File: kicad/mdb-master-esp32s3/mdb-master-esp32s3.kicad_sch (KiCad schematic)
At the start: 32 parts, among them J1 MDB_Connector, J2 Barrel_Jack, J3 USB_C_Receptacle_USB2.0_16P, J4 Conn_02x11_Odd_Even, Q1 BC807, SW1 SW_Push, U1 ESP32-S3R8, U2 AMS1117-3.3, Y1 40000hz

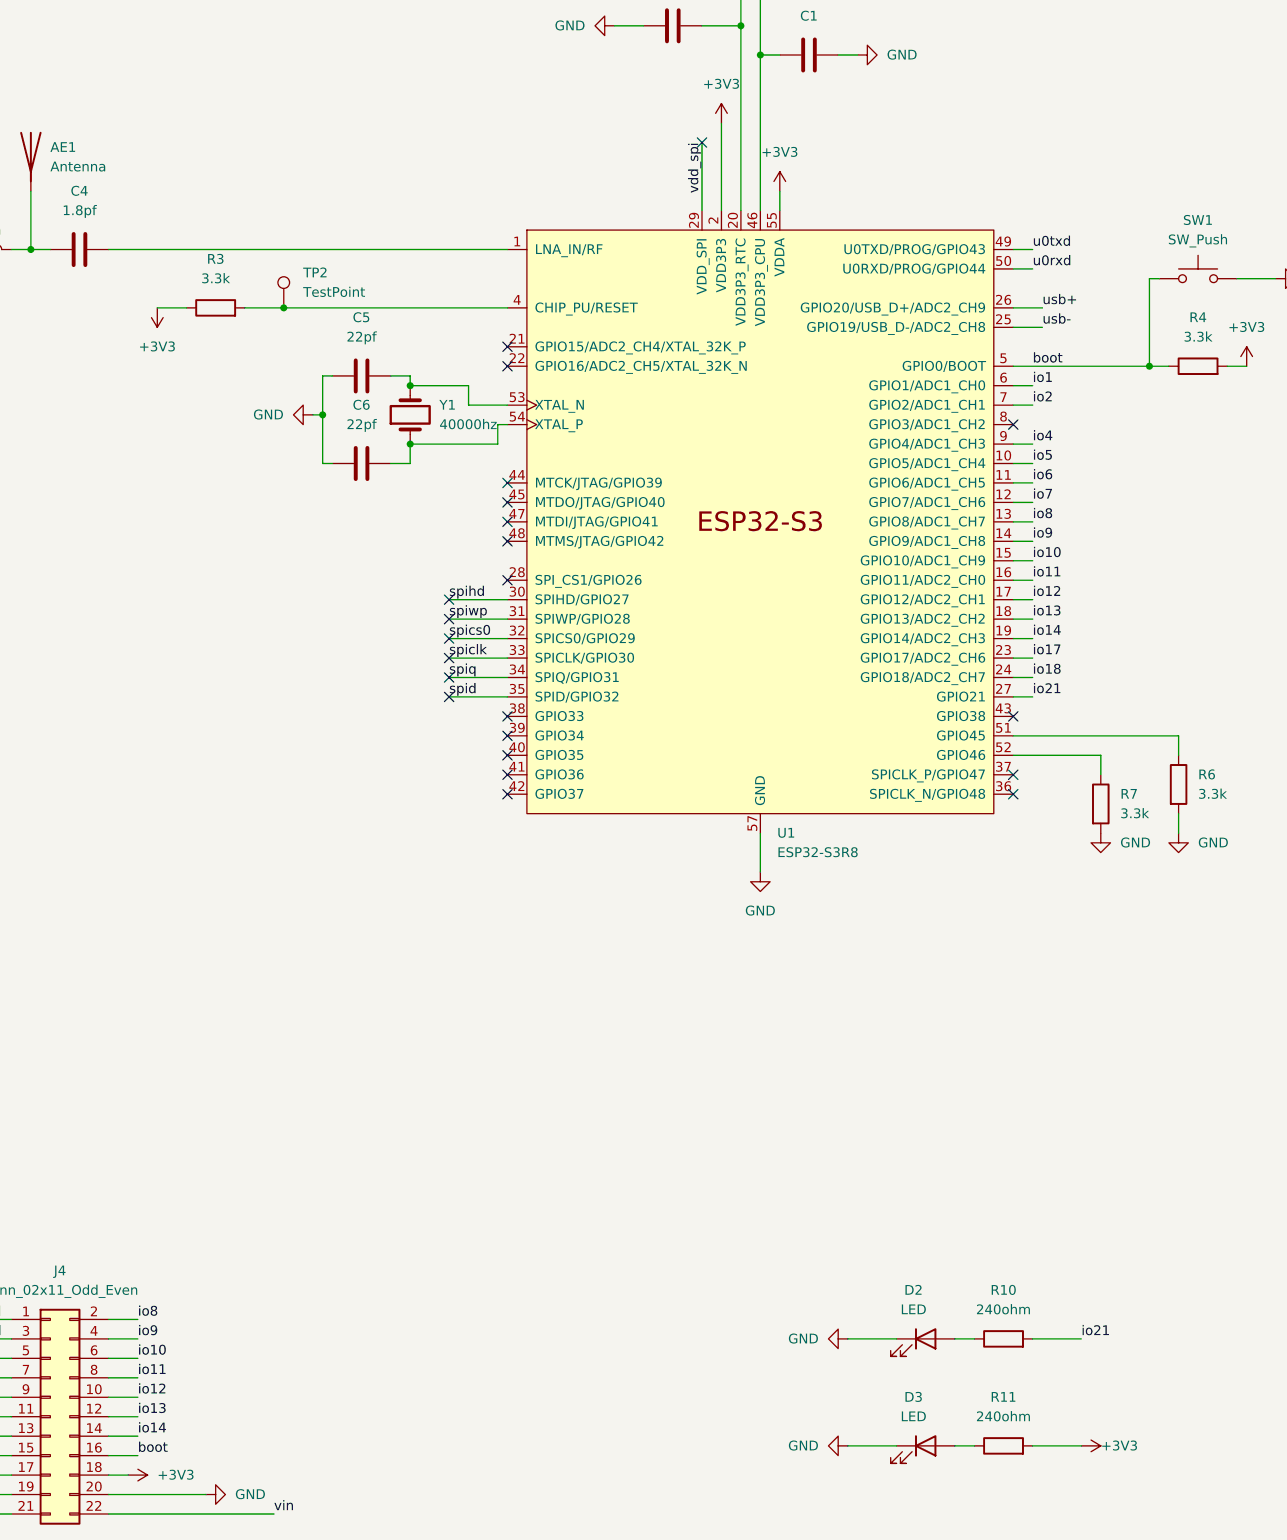
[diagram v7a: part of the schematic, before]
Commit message: Refacting Kicad layout
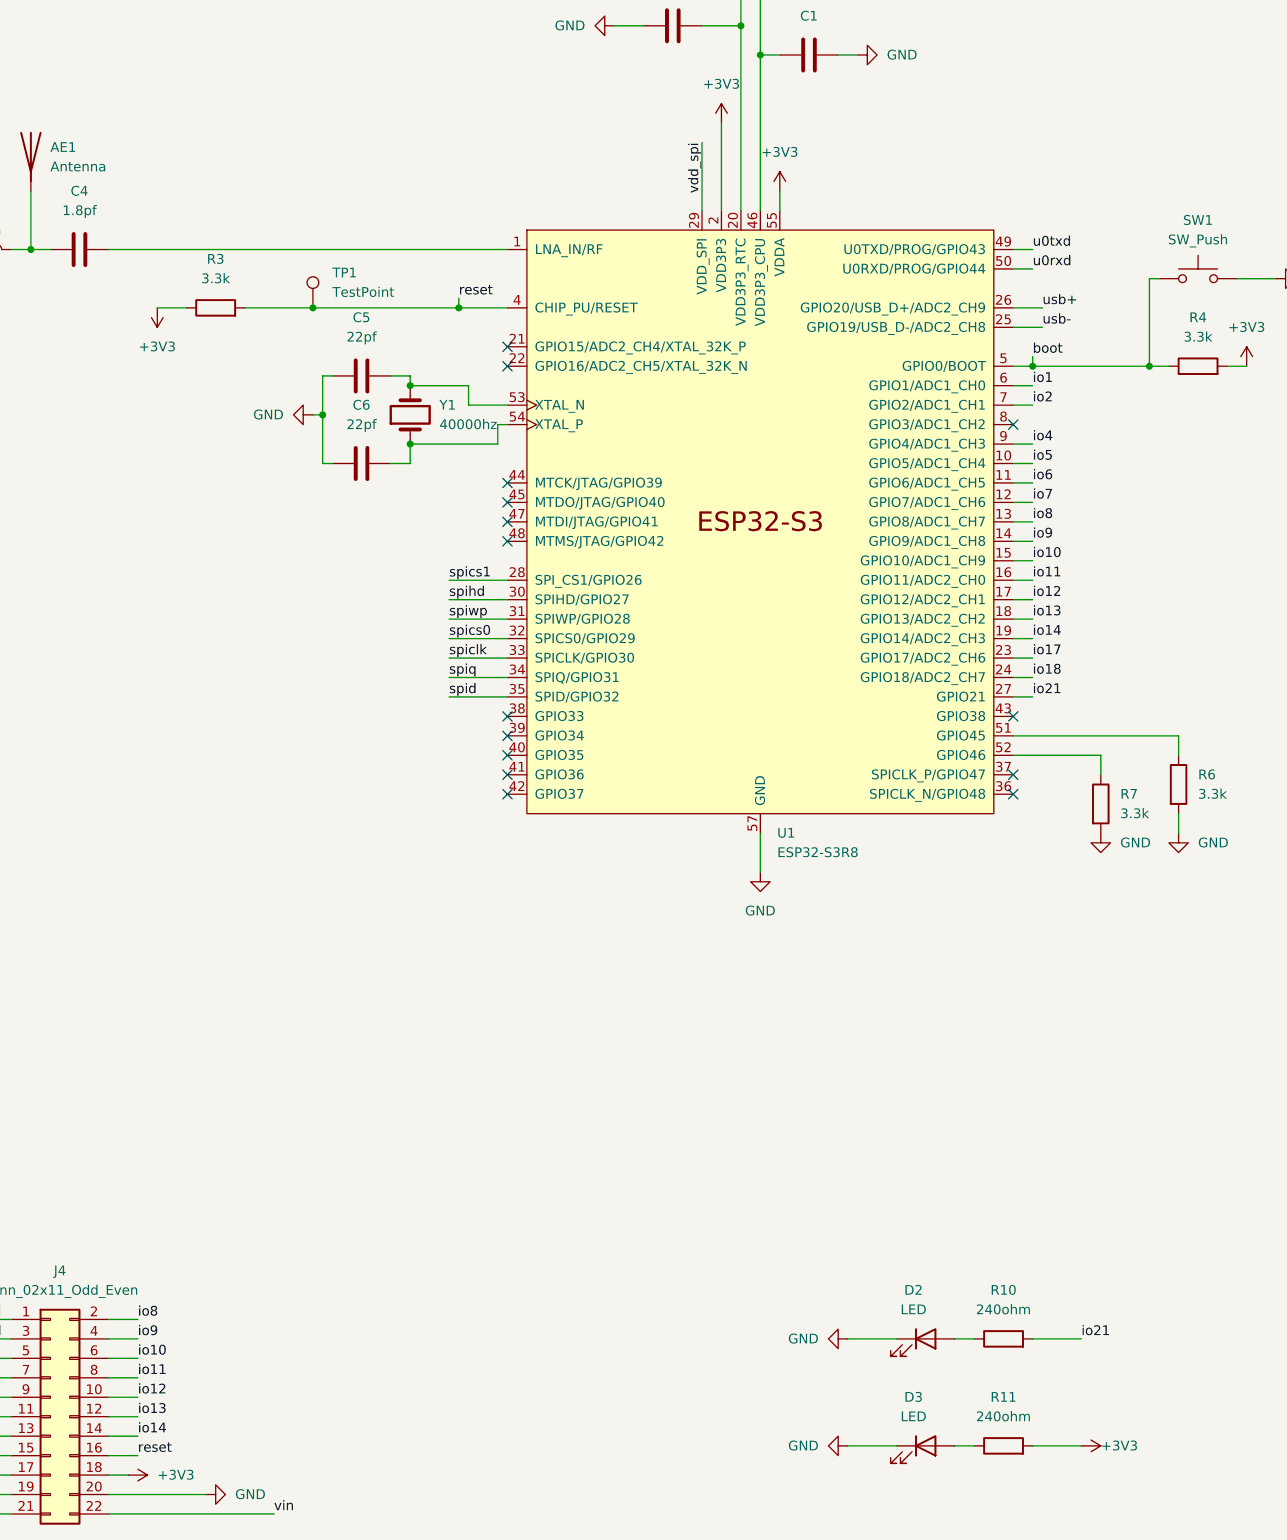
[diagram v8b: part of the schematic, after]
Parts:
- removed TP2: TestPoint, TestPoint:TestPoint_Pad_D1.0mm, symbol Connector:TestPoint
- added TP1: TestPoint, TestPoint:TestPoint_Pad_D1.0mm, symbol Connector:TestPoint
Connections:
- net boot: no longer J4.16 (Pin_16)
- net reset: now reaches R3.2, U1.4 (CHIP_PU/RESET)
- net reset: now also J4.16 (Pin_16), TP1.1
- net spics1: now reaches U1.28 (SPI_CS1/GPIO26)
- no-connect marks 26 -> 18
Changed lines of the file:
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@@
 	(paper "A3")
 	(junction
-		(at 102.87 107.95)
+		(at 184.15 105.41)
 		(diameter 0)
 		(color 0 0 0 0)
 	)
 	(junction
-		(at 320.04 196.85)
+		(at 102.87 107.95)
 		(diameter 0)
 		(color 0 0 0 0)
 	)
 	(junction
-		(at 86.36 97.79)
+		(at 320.04 196.85)
 		(diameter 0)
 		(color 0 0 0 0)
@@
 	)
 	(junction
+		(at 199.39 105.41)
+		(diameter 0)
+		(color 0 0 0 0)
+	)
+	(junction
 		(at 148.59 64.77)
 		(diameter 0)
@@
 	)
 	(junction
+		(at 109.22 97.79)
+		(diameter 0)
+		(color 0 0 0 0)
+	)
+	(junction
 		(at 91.44 111.76)
 		(diameter 0)
@@
 	)
 	(junction
-		(at 199.39 105.41)
+		(at 90.17 97.79)
 		(diameter 0)
 		(color 0 0 0 0)
@@
 	)
 	(no_connect
-		(at 107.95 138.43)
-	)
-	(no_connect
 		(at 115.57 156.21)
 	)
@@
 	)
 	(no_connect
-		(at 107.95 140.97)
-	)
-	(no_connect
-		(at 107.95 148.59)
-	)
-	(no_connect
-		(at 107.95 143.51)
-	)
-	(no_connect
 		(at 181.61 113.03)
 	)
@@
 	)
 	(no_connect
-		(at 115.57 133.35)
-	)
-	(no_connect
 		(at 115.57 102.87)
 	)
 	(no_connect
-		(at 140.97 76.2)
-	)
-	(no_connect
-		(at 107.95 135.89)
-	)
-	(no_connect
 		(at 181.61 161.29)
 	)
@@
 	)
 	(no_connect
-		(at 107.95 146.05)
-	)
-	(no_connect
 		(at 181.61 151.13)
 	)
@@
 	(wire
 		(pts
-			(xy 81.28 97.79) (xy 86.36 97.79)
-		)
-		(stroke
-			(width 0)
-			(type default)
-		)
-	)
-	(wire
-		(pts
 			(xy 44.45 245.11) (xy 50.8 245.11)
 		)
@@
 	(wire
 		(pts
-			(xy 86.36 97.79) (xy 115.57 97.79)
+			(xy 81.28 97.79) (xy 90.17 97.79)
 		)
 		(stroke
@@
 	(wire
 		(pts
+			(xy 184.15 104.14) (xy 184.15 105.41)
+		)
+		(stroke
+			(width 0)
+			(type default)
+		)
+	)
+	(wire
+		(pts
 			(xy 332.74 63.5) (xy 323.85 63.5)
 		)
@@
 	(wire
 		(pts
+			(xy 181.61 105.41) (xy 184.15 105.41)
+		)
+		(stroke
+			(width 0)
+			(type default)
+		)
+	)
+	(wire
+		(pts
 			(xy 100.33 118.11) (xy 102.87 118.11)
 		)
@@
 	(wire
 		(pts
-			(xy 181.61 105.41) (xy 199.39 105.41)
-		)
-		(stroke
-			(width 0)
-			(type default)
-		)
-	)
-	(wire
-		(pts
 			(xy 367.03 83.82) (xy 367.03 86.36)
 		)
@@
 	(wire
 		(pts
+			(xy 90.17 97.79) (xy 109.22 97.79)
+		)
+		(stroke
+			(width 0)
+			(type default)
+		)
+	)
+	(wire
+		(pts
 			(xy 166.37 246.38) (xy 160.02 246.38)
 		)
@@
 	(wire
 		(pts
+			(xy 107.95 133.35) (xy 115.57 133.35)
+		)
+		(stroke
+			(width 0)
+			(type default)
+		)
+	)
+	(wire
+		(pts
 			(xy 342.9 63.5) (xy 332.74 63.5)
 		)
@@
 	(wire
 		(pts
+			(xy 109.22 97.79) (xy 115.57 97.79)
+		)
+		(stroke
+			(width 0)
+			(type default)
+		)
+	)
+	(wire
+		(pts
 			(xy 332.74 196.85) (xy 331.47 196.85)
 		)
@@
 	(wire
 		(pts
+			(xy 109.22 96.52) (xy 109.22 97.79)
+		)
+		(stroke
+			(width 0)
+			(type default)
+		)
+	)
+	(wire
+		(pts
+			(xy 184.15 105.41) (xy 199.39 105.41)
+		)
+		(stroke
+			(width 0)
+			(type default)
+		)
+	)
+	(wire
+		(pts
 			(xy 44.45 252.73) (xy 50.8 252.73)
 		)
@@
 		)
 	)
+	(label "spics1"
+		(at 107.95 133.35 0)
+		(fields_autoplaced yes)
+		(effects
+			(font
+				(size 1.27 1.27)
+			)
+			(justify left bottom)
+		)
+	)
 	(label "io8"
 		(at 184.15 125.73 0)
@@
 	)
 	(label "boot"
-		(at 184.15 105.41 0)
+		(at 184.15 104.14 0)
 		(fields_autoplaced yes)
 		(effects
@@
 		)
 	)
-	(label "boot"
-		(at 67.31 247.65 0)
+	(label "io4"
+		(at 184.15 115.57 0)
 		(fields_autoplaced yes)
 		(effects
@@
 		)
 	)
-	(label "io4"
-		(at 184.15 115.57 0)
+	(label "reset"
+		(at 67.31 247.65 0)
 		(fields_autoplaced yes)
 		(effects
@@
 		)
 	)
+	(label "reset"
+		(at 109.22 96.52 0)
+		(fields_autoplaced yes)
+		(effects
+			(font
+				(size 1.27 1.27)
+			)
+			(justify left bottom)
+		)
+	)
 	(label "io9"
 		(at 184.15 128.27 0)
@@
 	)
 	(symbol
+		(lib_id "Connector:TestPoint")
+		(at 90.17 97.79 0)
+		(unit 1)
+		(exclude_from_sim no)
+		(in_bom yes)
+		(on_board yes)
+		(dnp no)
+		(fields_autoplaced yes)
+		(property "Reference" "TP1"
+			(at 92.71 93.2179 0)
+			(effects
+				(font
+					(size 1.27 1.27)
+				)
+				(justify left)
+			)
+		)
+		(property "Value" "TestPoint"
+			(at 92.71 95.7579 0)
+			(effects
+				(font
+					(size 1.27 1.27)
+				)
+				(justify left)
+			)
+		)
+		(property "Footprint" "TestPoint:TestPoint_Pad_D1.0mm"
+			(at 95.25 97.79 0)
+			(effects
+				(font
+					(size 1.27 1.27)
+				)
+				(hide yes)
+			)
+		)
+		(property "Datasheet" "~"
+			(at 95.25 97.79 0)
+			(effects
+				(font
+					(size 1.27 1.27)
+				)
+				(hide yes)
+			)
+		)
+		(property "Description" "test point"
+			(at 90.17 97.79 0)
+			(effects
+				(font
+					(size 1.27 1.27)
+				)
+				(hide yes)
+			)
+		)
+		(pin "1"
+		)
+		(instances
+			(project ""
+				(path "/1a9a25ce-6784-46e5-b680-57f383f3a43d"
+					(reference "TP1")
+					(unit 1)
+				)
+			)
+		)
+	)
+	(symbol
 		(lib_id "power:+3V3")
 		(at 66.04 250.19 270)
@@
 					(unit 1)
 				)
-			)
-		)
-	)
-	(symbol
-		(lib_id "Connector:TestPoint")
-		(at 86.36 97.79 0)
-		(unit 1)
-		(exclude_from_sim no)
-		(in_bom yes)
-		(on_board yes)
-		(dnp no)
-		(fields_autoplaced yes)
-		(property "Reference" "TP2"
-			(at 88.9 93.2179 0)
-			(effects
-				(font
-					(size 1.27 1.27)
-				)
-				(justify left)
-			)
-		)
-		(property "Value" "TestPoint"
-			(at 88.9 95.7579 0)
-			(effects
-				(font
-					(size 1.27 1.27)
-				)
-				(justify left)
-			)
-		)
-		(property "Footprint" "TestPoint:TestPoint_Pad_D1.0mm"
-			(at 91.44 97.79 0)
-			(effects
-				(font
-					(size 1.27 1.27)
-				)
-				(hide yes)
-			)
-		)
-		(property "Datasheet" "~"
-			(at 91.44 97.79 0)
-			(effects
-				(font
-					(size 1.27 1.27)
-				)
-				(hide yes)
-			)
-		)
-		(property "Description" "test point"
-			(at 86.36 97.79 0)
-			(effects
-				(font
-					(size 1.27 1.27)
-				)
-				(hide yes)
-			)
-		)
-		(pin "1"
-		)
-		(instances
-			(project "mdb-master-esp32s3"
-				(path "/1a9a25ce-6784-46e5-b680-57f383f3a43d"
-					(reference "TP2")
-					(unit 1)
-				)
